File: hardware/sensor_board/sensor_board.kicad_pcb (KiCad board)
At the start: 2 copper layers, 88 parts, among them IC1 ATMEGA88A-A, J1 RJ45_8P8C_8FACH, K1 pow_sel, P1 UART, P2 Shield, P3 i2c_pow, P4 i2c_chain, P5 12Vin, P6 HOHLBUCHSE, P7 Vccin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

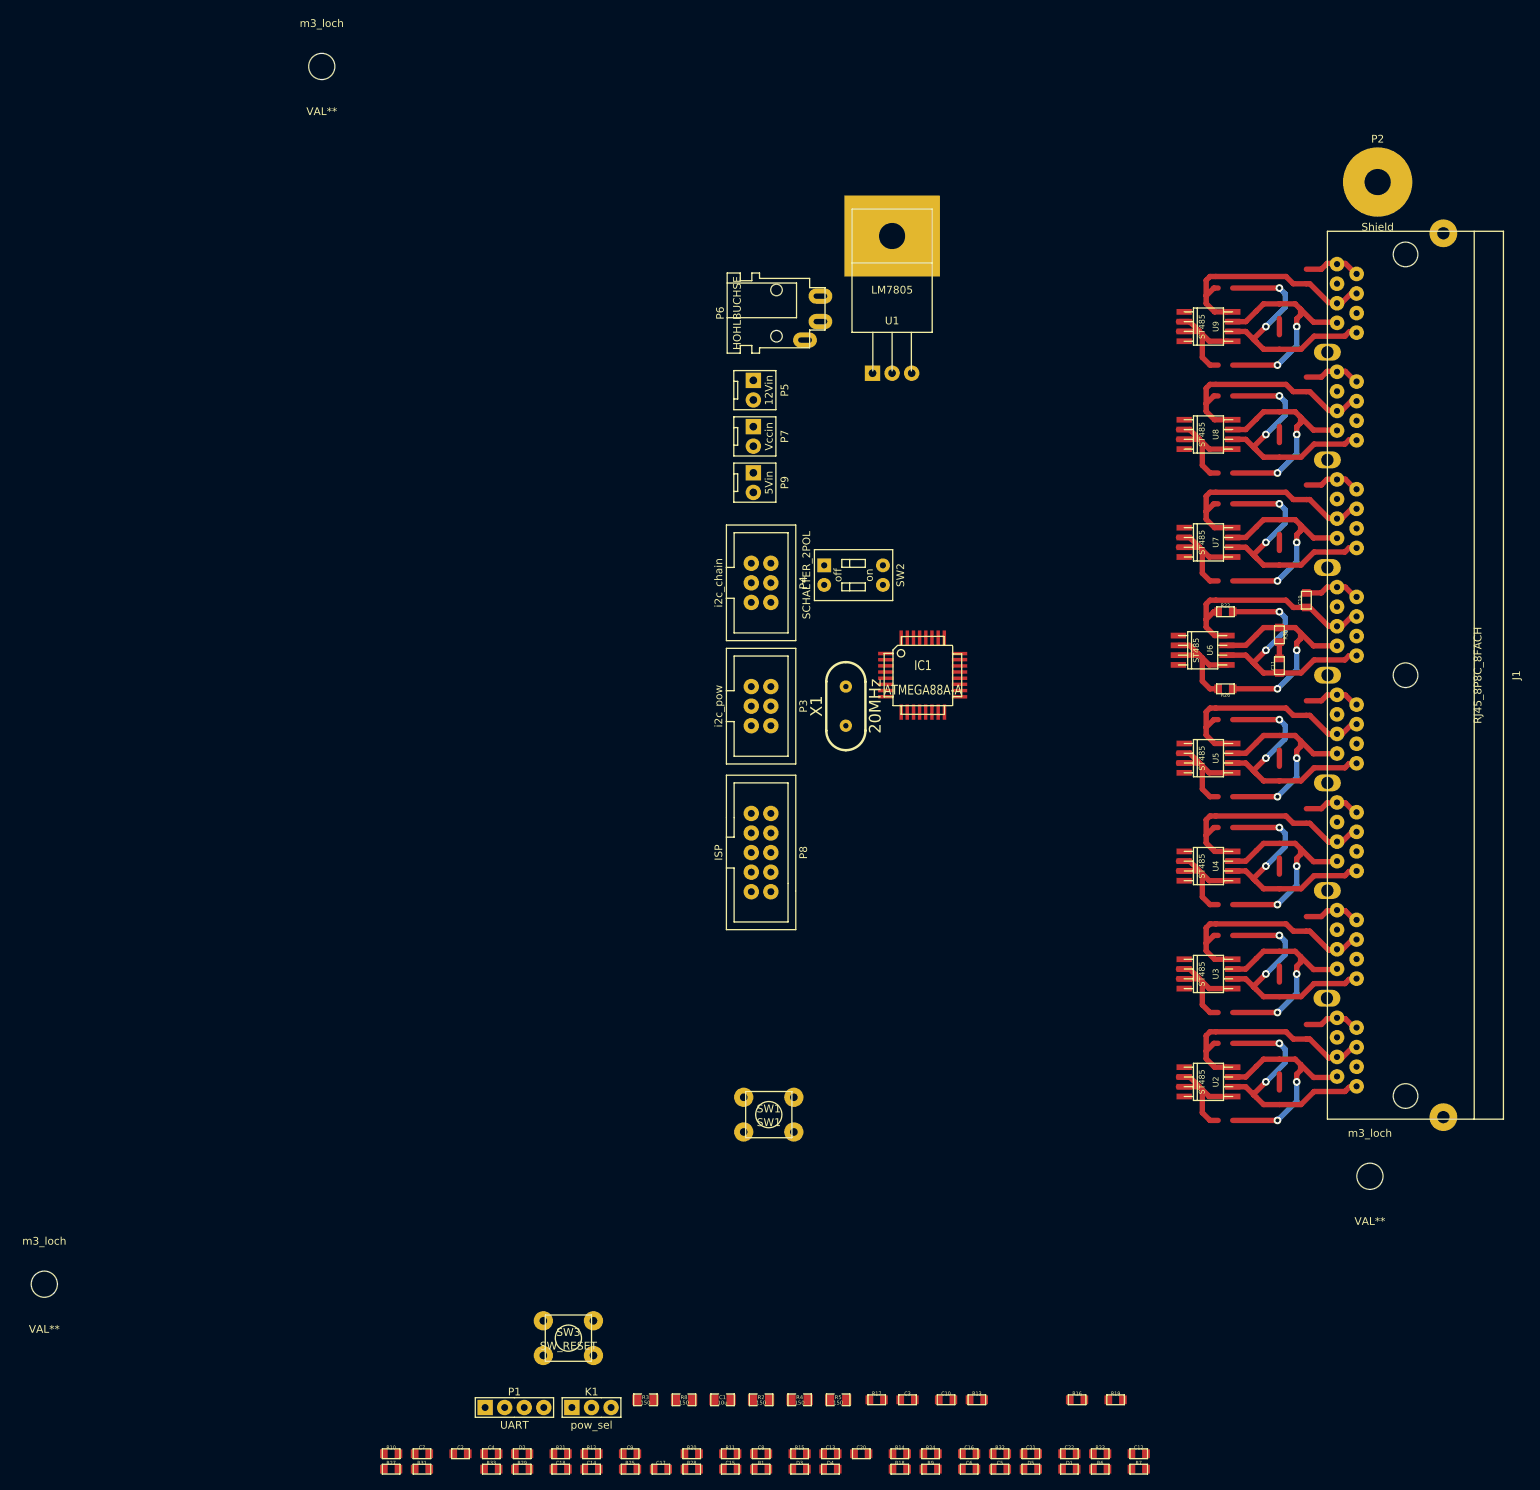
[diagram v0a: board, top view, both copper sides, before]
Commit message: sensor board pcb routing started
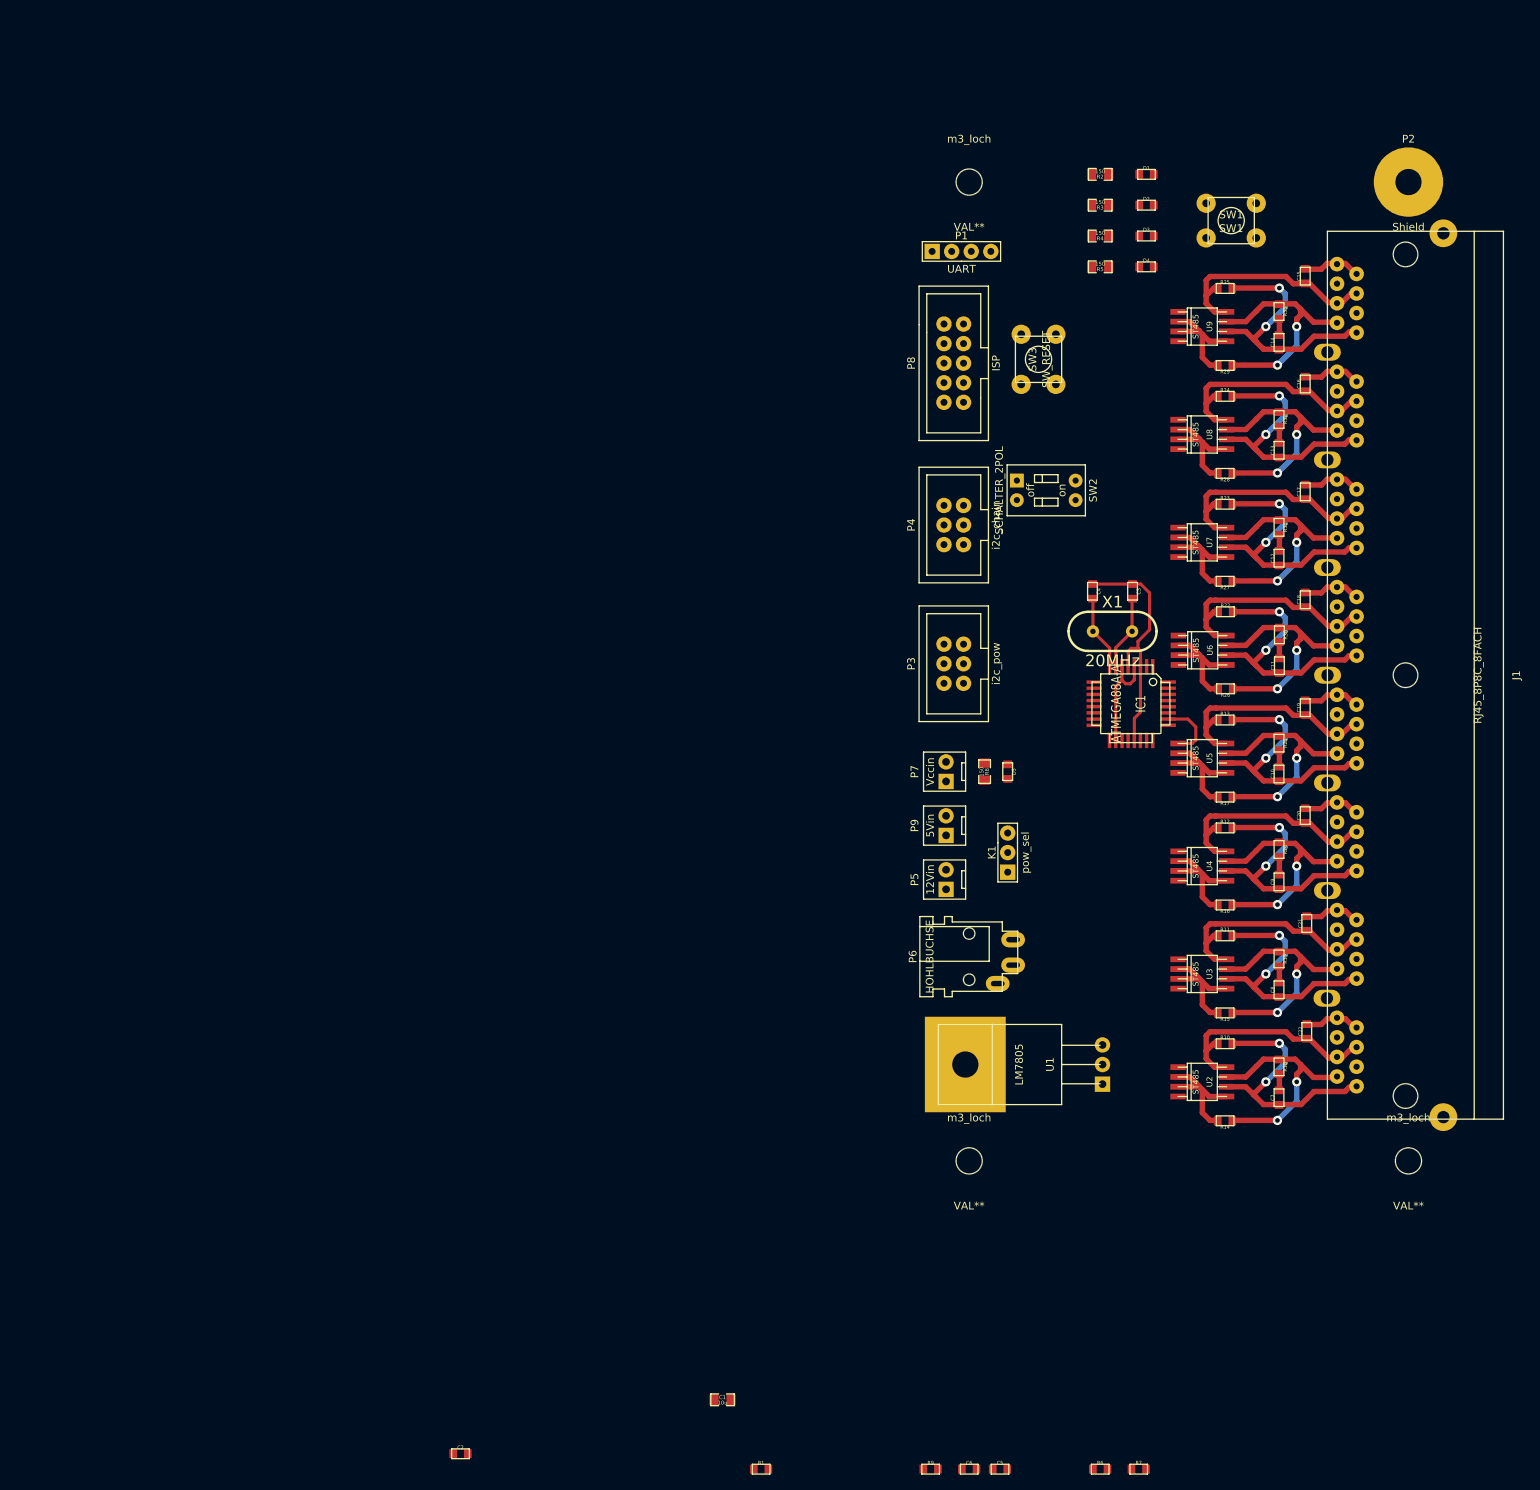
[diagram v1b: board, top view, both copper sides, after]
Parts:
- D3: value LED1 -> LED3
- D4: value LED2 -> LED4
- moved R33 181.7 mm to (238.2, 65.8), turned to 270 degrees
- moved D2 181.1 mm to (221.0, 52.0)
- moved C15 171.8 mm to (241.6, 61.2), turned to 90 degrees
- moved R25 171.6 mm to (231.2, 62.8)
- moved C14 171.3 mm to (238.2, 69.8), turned to 90 degrees
- moved R29 169.8 mm to (231.2, 72.8), turned to 180 degrees
- moved D1 168.3 mm to (221.0, 48.0)
- moved D3 166.2 mm to (221.0, 56.0)
- moved R3 165.8 mm to (215.0, 52.0), turned to 180 degrees
- moved R31 165.2 mm to (238.2, 93.8), turned to 270 degrees
- moved R2 165.0 mm to (215.0, 48.0), turned to 180 degrees
- moved D4 161.3 mm to (221.0, 60.0)
- moved P1 160.8 mm to (197.0, 58.0)
- moved R27 158.0 mm to (231.2, 100.8), turned to 180 degrees
- moved R4 156.0 mm to (215.0, 56.0), turned to 180 degrees
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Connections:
- IC1 pad 10: /LED4 -> /SW1
- IC1 pad 11: /SW1 -> /LED4
- IC1 pad 12: /LED1 -> /LED3
- IC1 pad 14: /LED3 -> /LED1
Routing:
- net GND: track 184.8 -> 216.3 mm
- net (no net): track 14.8 -> 0.00 mm
- net VCC: track 238.2 -> 251.8 mm
- net /XTAL2: track 0.00 -> 9.76 mm
- net /XTAL1: track 0.00 -> 9.74 mm
- net /ZAC_04: track 0.00 -> 8.18 mm
- net N-0000087: track 0.00 -> 2.11 mm
- net N-0000086: track 0.00 -> 2.11 mm
- net N-0000085: track 0.00 -> 2.11 mm
- net N-000007: track 0.00 -> 2.11 mm
- net N-0000066: track 0.00 -> 2.11 mm
- net N-000004: track 0.00 -> 2.11 mm
- net N-0000019: track 0.00 -> 2.11 mm
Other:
- net class Default: via_dia 1 -> 1.2
- net class uc added: clearance 0.254, trace_width 0.4, via_dia 1.2, via_drill 0.6

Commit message: sensor_board: all connected
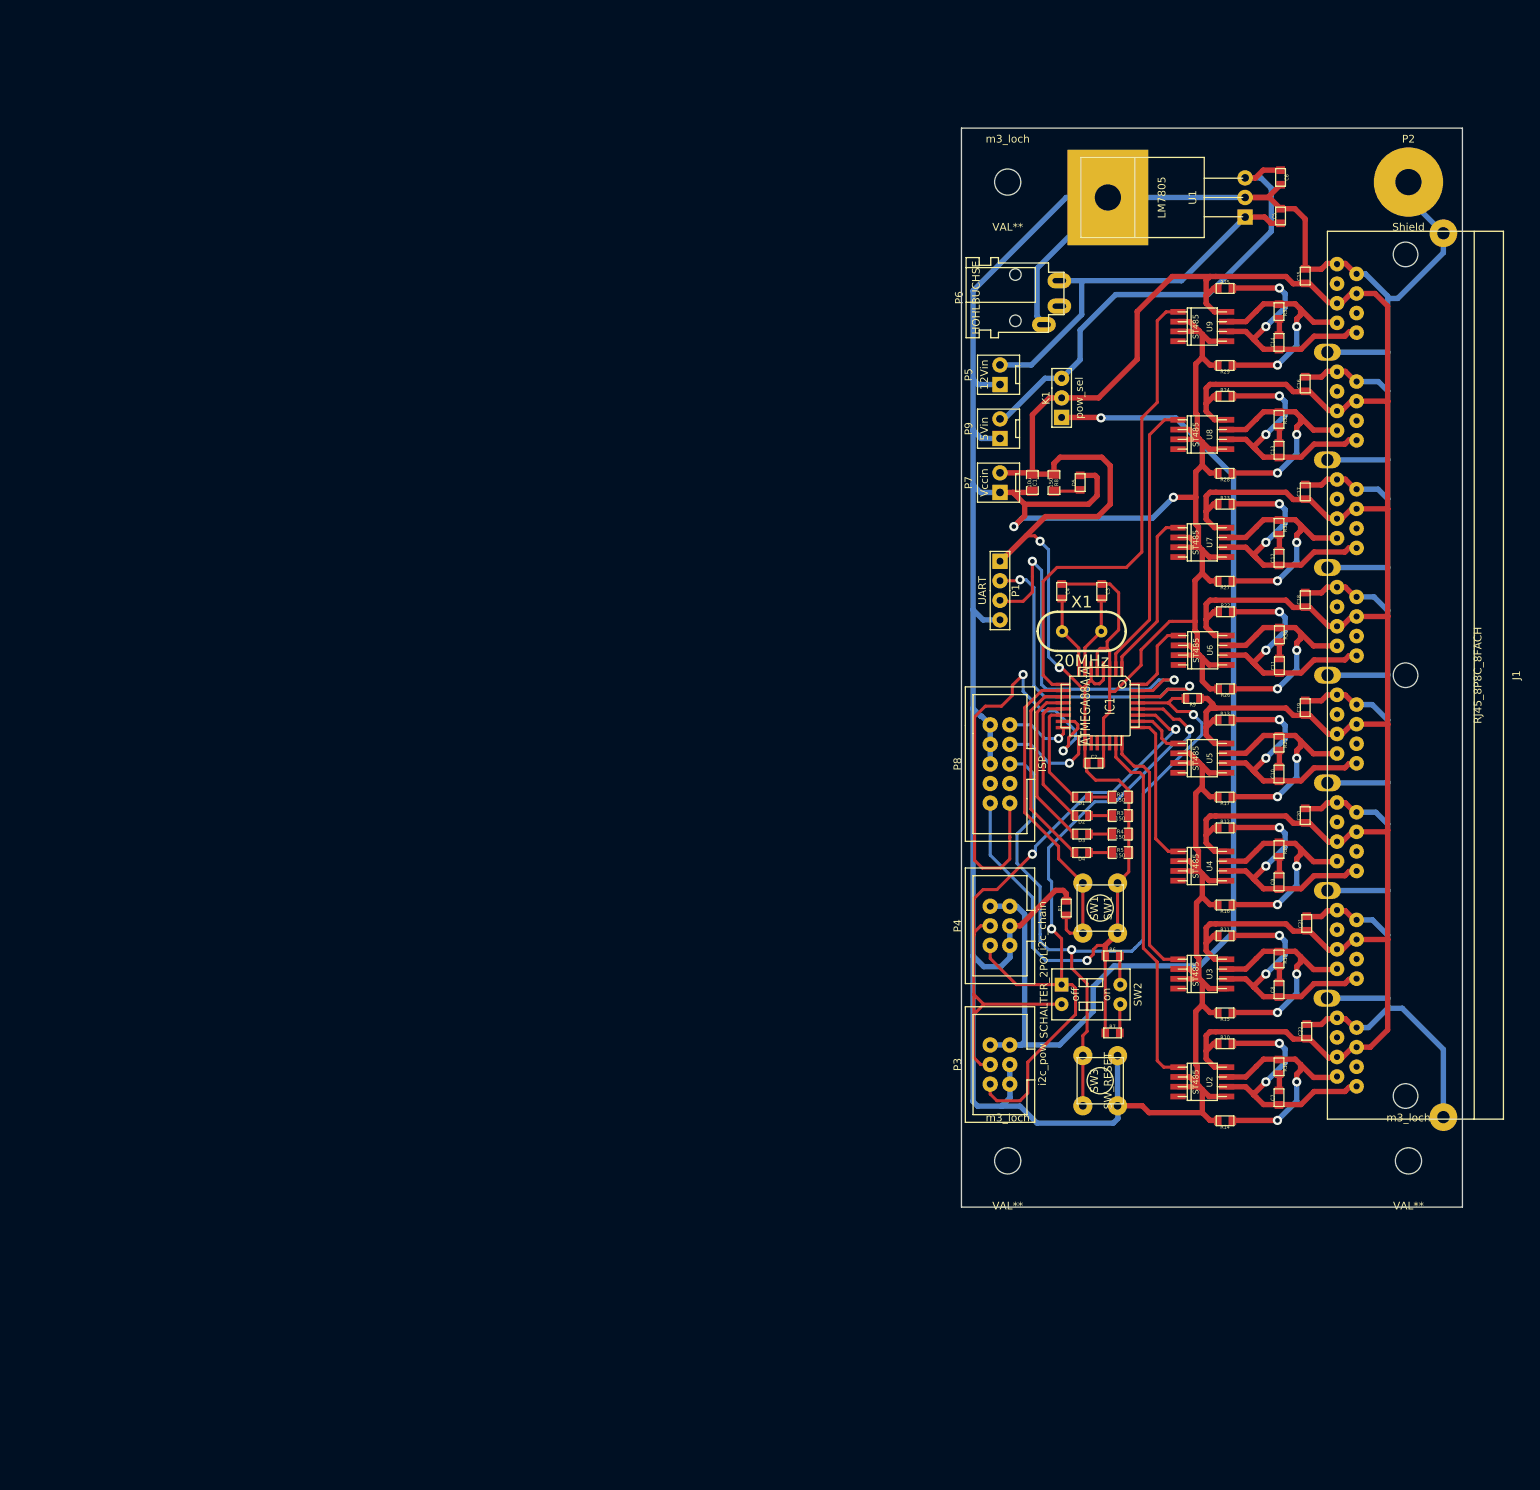
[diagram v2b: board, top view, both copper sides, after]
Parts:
- moved C6 172.4 mm to (238.4, 48.4), turned to 270 degrees
- moved C5 166.6 mm to (238.4, 53.4), turned to 90 degrees
- moved C1 125.6 mm to (206.2, 88.0), turned to 270 degrees
- moved C2 121.6 mm to (214.2, 124.4)
- moved U1 114.0 mm to (216.0, 51.0)
- moved R9 105.6 mm to (227.0, 116.0), turned to 180 degrees
- moved SW3 93.9 mm to (215.0, 165.6)
- moved SW1 90.8 mm to (215.0, 143.2), turned to 90 degrees
- moved P6 85.7 mm to (204.0, 64.0)
- moved R1 82.9 mm to (210.6, 143.2), turned to 90 degrees
- moved D1 81.2 mm to (212.6, 128.8), turned to 180 degrees
- moved R2 80.8 mm to (217.6, 128.8), turned to 0 degrees
- moved D2 79.6 mm to (212.6, 131.2), turned to 180 degrees
- moved R3 79.2 mm to (217.6, 131.2), turned to 0 degrees
- moved D3 78.1 mm to (212.6, 133.6), turned to 180 degrees
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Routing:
- net GND: track 216.3 -> 854.1 mm, vias 0 -> 2
- net VCC: track 251.8 -> 563.9 mm, vias 0 -> 3
- net /Vi2c: track 0.00 -> 146.2 mm, vias 0 -> 1
- net /RESET: track 0.00 -> 106.6 mm, vias 0 -> 2
- net /SCL: track 0.00 -> 89.0 mm, vias 0 -> 2
- net /SDA: track 0.00 -> 81.2 mm, vias 0 -> 2
- net /ZAC_08: track 0.00 -> 63.7 mm
- net /Vreg: track 0.00 -> 62.1 mm
- net /MOSI: track 0.00 -> 61.3 mm, vias 0 -> 2
- net +12V: track 0.00 -> 50.2 mm
- net /TX: track 0.00 -> 48.5 mm, vias 0 -> 2
- net /ZAC_01: track 0.00 -> 47.2 mm
- net /RX: track 0.00 -> 46.4 mm, vias 0 -> 2
- net /SW1: track 0.00 -> 42.5 mm
- net /ZAC_07: track 0.00 -> 36.7 mm
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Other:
- board outline added: 65 x 140 mm
